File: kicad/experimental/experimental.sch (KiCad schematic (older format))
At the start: 0 parts

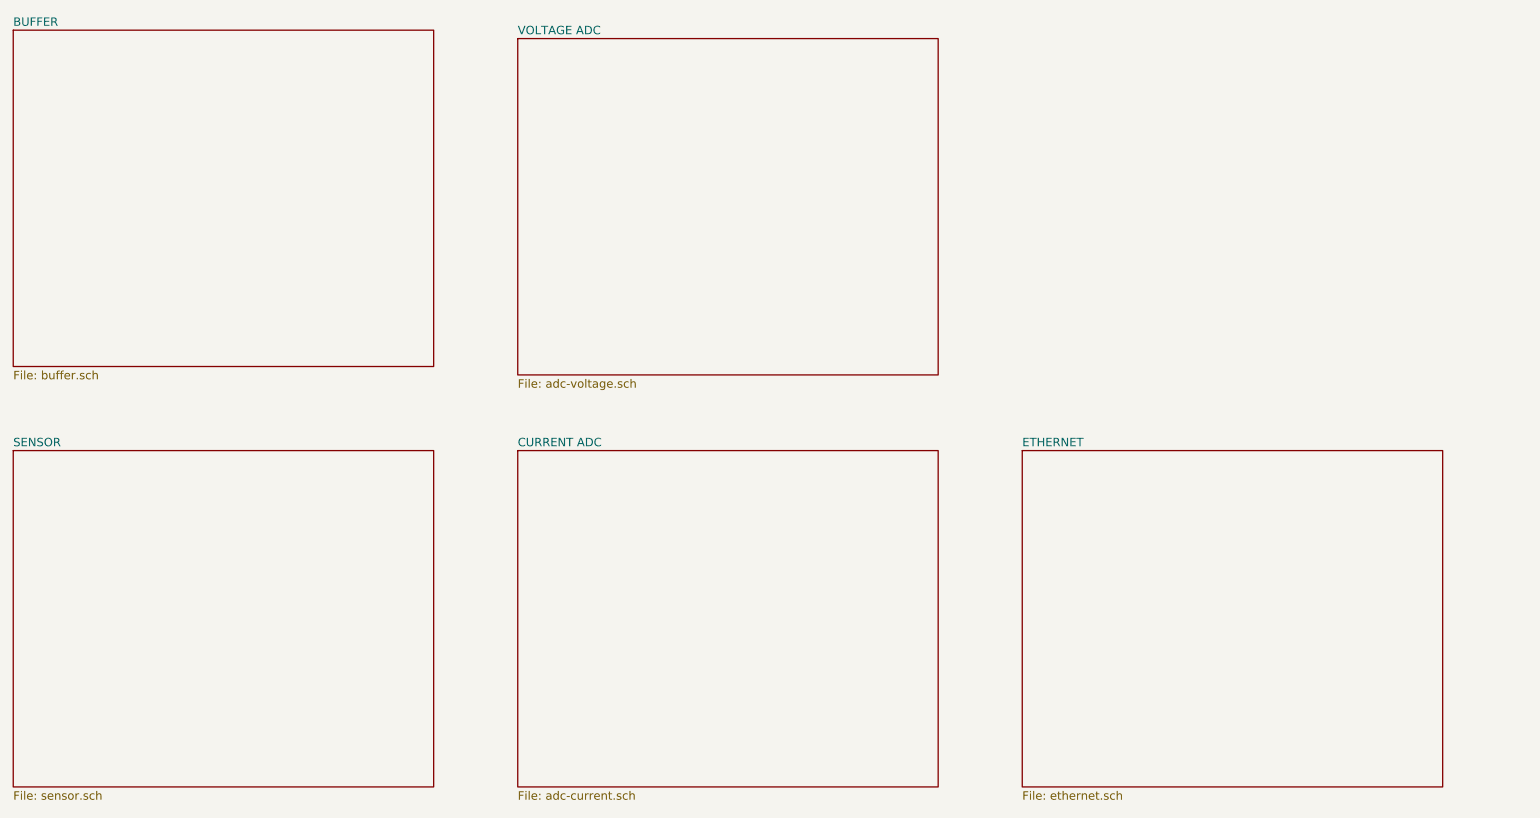
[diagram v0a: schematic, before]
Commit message: removed current adc components from experimental kicad design
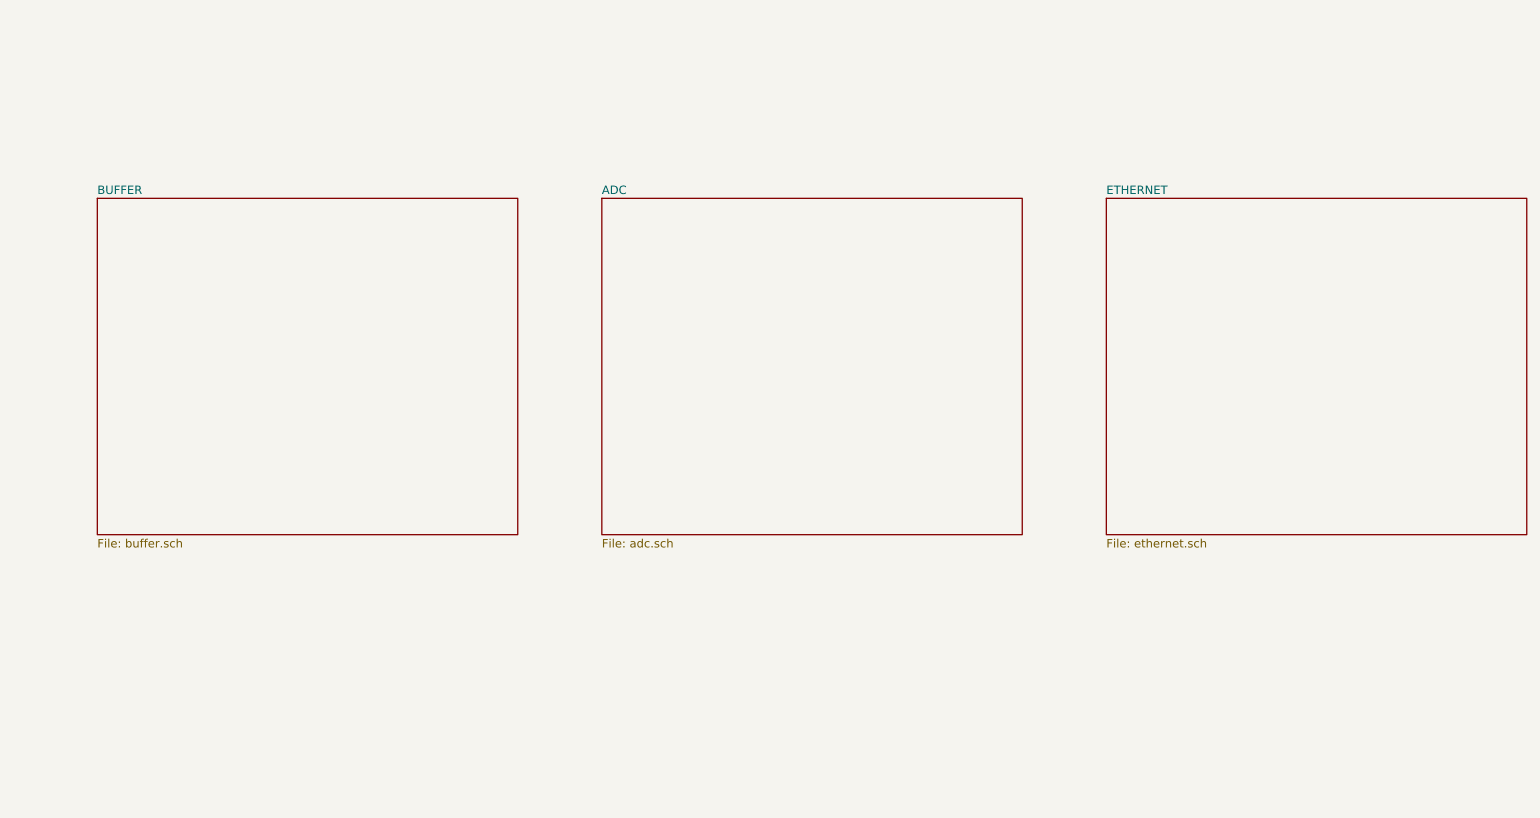
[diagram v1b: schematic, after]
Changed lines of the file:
@@
 $Descr A4 11693 8268
 encoding utf-8
-Sheet 1 5
+Sheet 1 4
 Title ""
 Date ""
@@
 $EndDescr
 $Sheet
-S 4000 4000 2500 2000
-U 5D60153C
-F0 "CURRENT ADC" 50
-F1 "adc-current.sch" 50
-$EndSheet
-$Sheet
-S 4000 1550 2500 2000
-U 5D601578
-F0 "VOLTAGE ADC" 50
-F1 "adc-voltage.sch" 50
-$EndSheet
-$Sheet
-S 1000 4000 2500 2000
-U 5D60196C
-F0 "SENSOR" 50
-F1 "sensor.sch" 50
-$EndSheet
-$Sheet
-S 7000 4000 2500 2000
+S 7500 2500 2500 2000
 U 5D601C3B
 F0 "ETHERNET" 50
@@
 $EndSheet
 $Sheet
-S 1000 1500 2500 2000
+S 1500 2500 2500 2000
 U 5D61C196
 F0 "BUFFER" 50
 F1 "buffer.sch" 50
 $EndSheet
+$Sheet
+S 4500 2500 2500 2000
+U 5D601578
+F0 "ADC" 50
+F1 "adc.sch" 50
+$EndSheet
 $EndSCHEMATC
